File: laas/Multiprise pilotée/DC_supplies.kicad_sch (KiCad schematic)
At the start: 22 parts, among them J7 Conn_02x06_Odd_Even, Q1 DMN2020LSN-7, Q2 DMN2020LSN-7, Q3 SSM3J355R,LF, Q4 DMN2020LSN-7, Q5 DMN2020LSN-7, Q6 SSM3J355R,LF, Q7 DMN2020LSN-7, Q8 DMN2020LSN-7, U2 74HC595, U4 TC4469, U5 TC4469, U6 TDA7391PD, U7 74AHC1G08

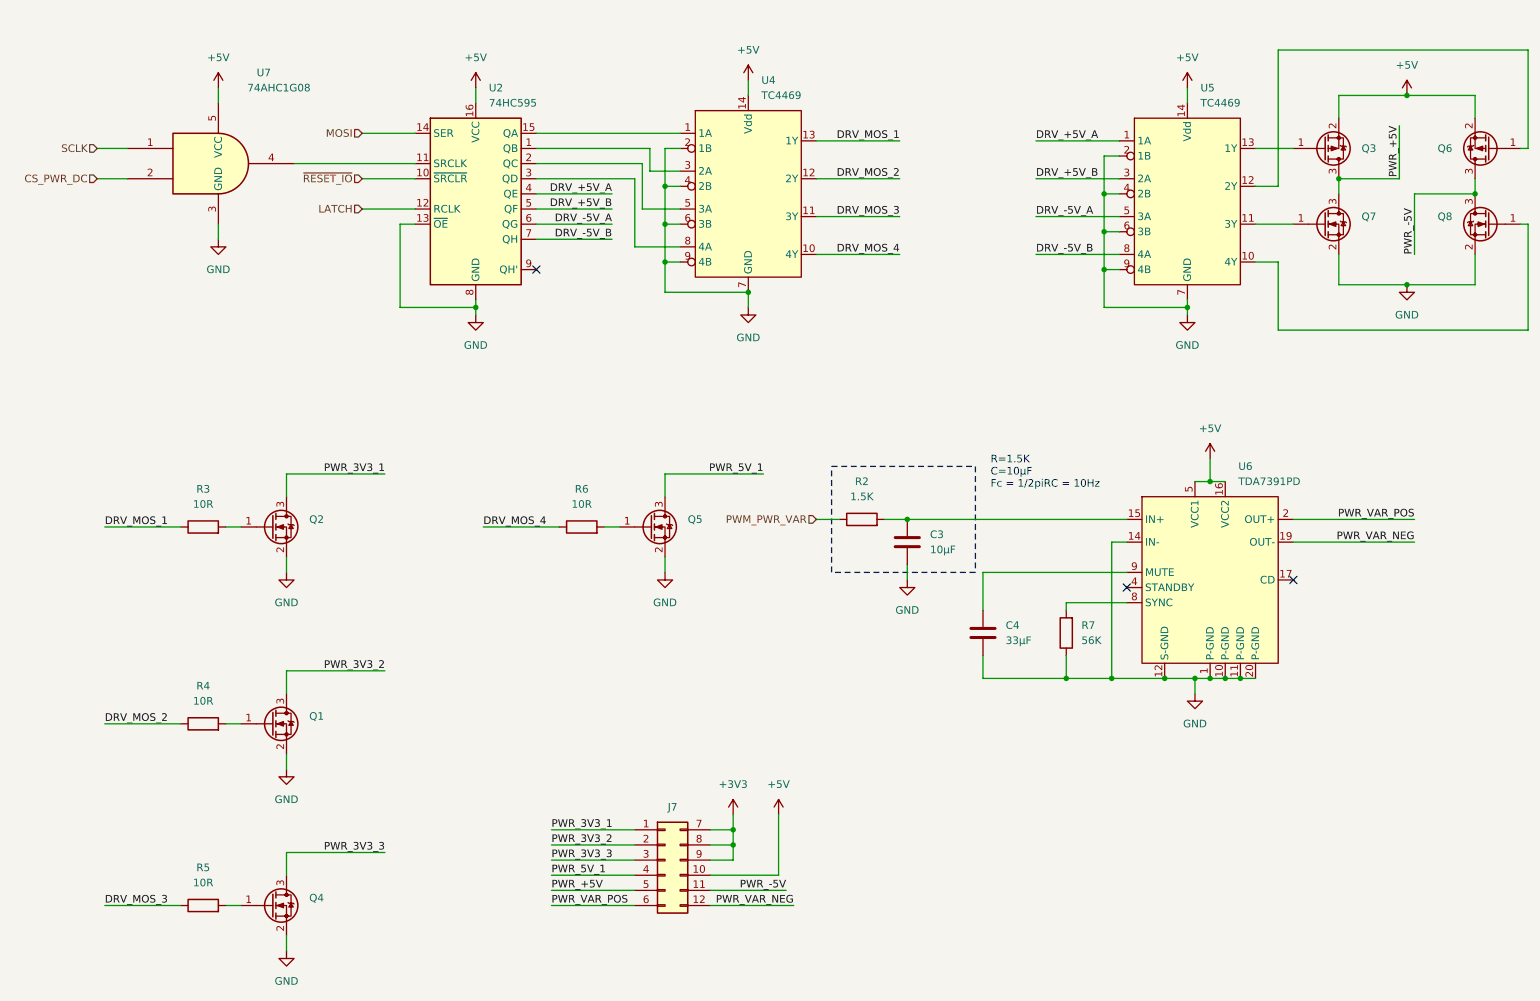
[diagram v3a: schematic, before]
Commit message: Nouvelle version PCB multiprise 1.3 avec suppresion des alim vpol et var
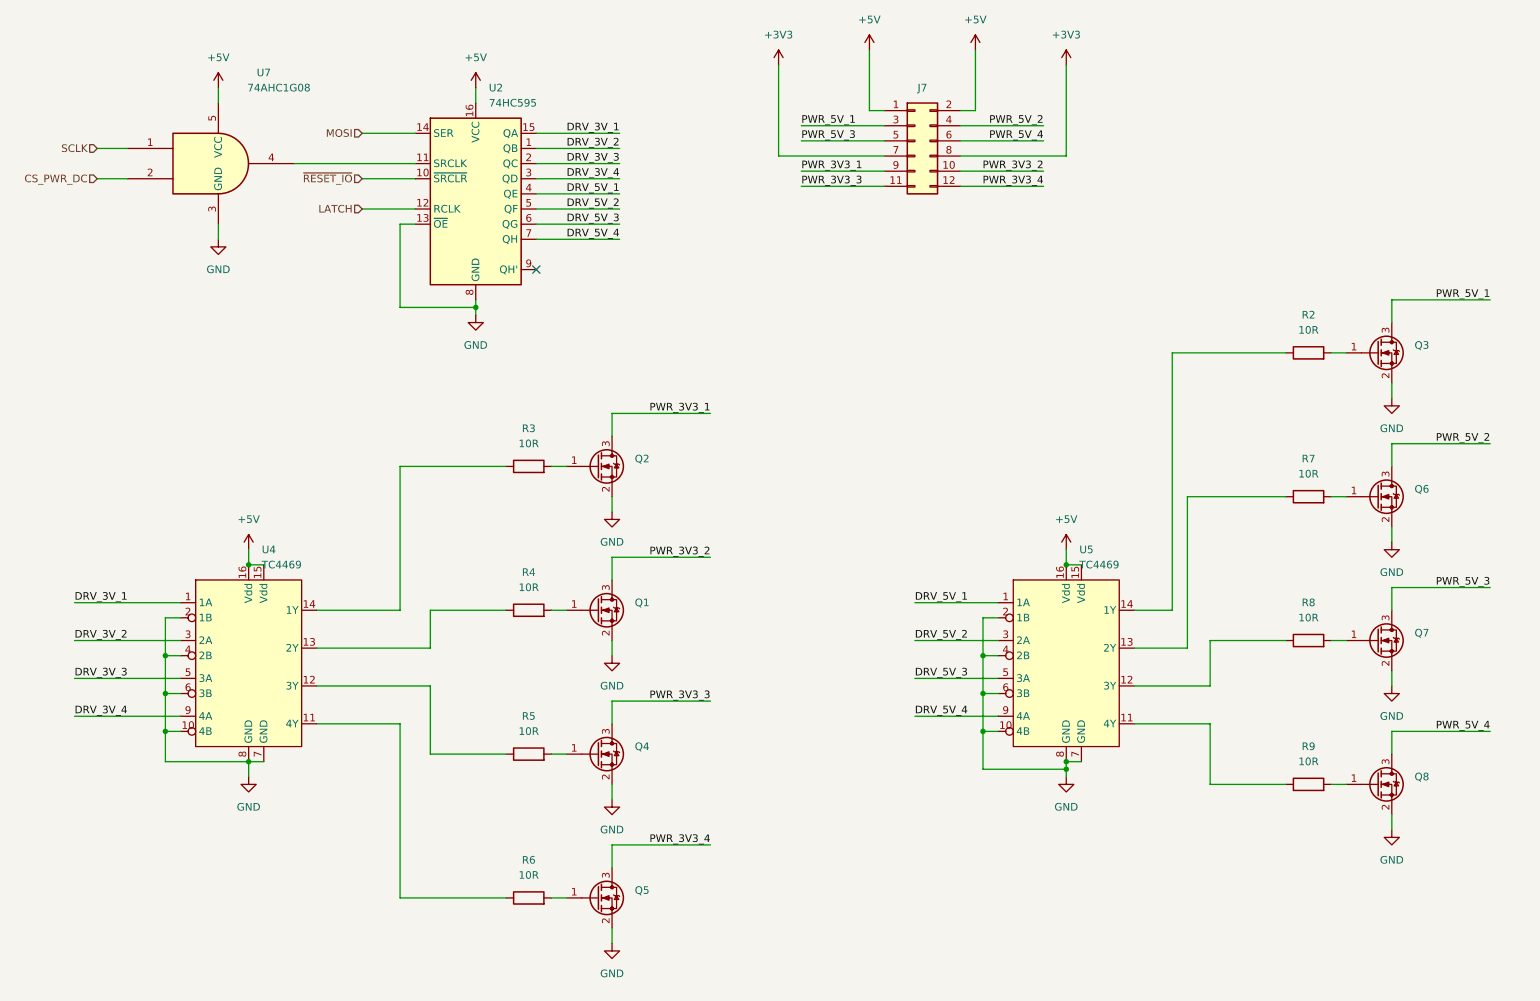
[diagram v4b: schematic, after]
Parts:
- removed C3: 10µF, Capacitor_SMD:C_1206_3216Metric, symbol Device:C
- removed C4: 33µF, Capacitor_SMD:C_1206_3216Metric, symbol Device:C
- removed Q3, Q6: SSM3J355R,LF, Package_TO_SOT_SMD:SOT-23, symbol Device:Q_PMOS_GSD
- removed U6: TDA7391PD, footprints:SO_91PDTR_STM, symbol Multiprise pilotée:TDA7391PD
- added Q3, Q6: DMN2020LSN-7, Package_TO_SOT_SMD:SC-59, symbol Device:Q_NMOS_GSD
- added R8, R9: 10R, Resistor_SMD:R_1206_3216Metric, symbol Device:R
- J7: footprint Borniers:M80-85312YY -> Connector_PinSocket_2.54mm:PinSocket_2x06_P2.54mm_Horizontal; symbol Connector_Generic:Conn_02x06_Top_Bottom -> Connector_Generic:Conn_02x06_Odd_Even
- Q1, Q2, Q4, Q5, Q7, Q8: value DMN2020LSN-7 -> DMN2020LSN-7
- R2: value 1.5K -> 10R
- R7: value 56K -> 10R
- U4, U5: footprint Package_SO:SOIC-14W_7.5x9mm_P1.27mm -> Package_SO:SOIC-16W_7.5x10.3mm_P1.27mm
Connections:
- net PWR_VAR_POS is gone; now on net PWR_5V_4: J7.6 (Pin_6)
- net +3V3: no longer J7.9 (Pin_9)
- net +5V: now also J7.1 (Pin_1), J7.2 (Pin_2), U4.15 (Vdd), U4.16 (Vdd), U5.15 (Vdd), U5.16 (Vdd); no longer J7.10 (Pin_10), U4.14 (Vdd), U5.14 (Vdd)
- net GND: now also U4.10 (4B), U4.8 (GND), U5.10 (4B), U5.8 (GND), Q3.2 (S), Q6.2 (S); no longer R7.1, U4.9 (4B), U5.9 (4B)
- net PWR_3V3_1: now also J7.9 (Pin_9); no longer J7.1 (Pin_1)
- net PWR_3V3_2: now also J7.10 (Pin_10); no longer J7.2 (Pin_2)
- net PWR_3V3_3: now also J7.11 (Pin_11); no longer J7.3 (Pin_3)
- net PWR_5V_1: now also J7.3 (Pin_3), Q3.3 (D); no longer J7.4 (Pin_4), Q5.3 (D)
- net at R7.2: now also Q6.1 (G)
- net at R2.2: now also Q3.1 (G)
- net DRV_3V_2: now reaches U2.1 (QB), U4.3 (2A)
- net DRV_3V_1: now reaches U2.15 (QA), U4.1 (1A)
- net DRV_3V_3: now reaches U2.2 (QC), U4.5 (3A)
- net DRV_3V_4: now reaches U2.3 (QD)
- net DRV_3V_4: now also U4.9 (4A); no longer U4.8 (4A)
- net at U5.12 (3Y): now also R8.1
- net at Q8.1 (G): now also R9.2; no longer U5.10 (4Y)
- net at Q7.1 (G): now also R8.2; no longer U5.11 (3Y)
- net at U5.13 (2Y): now also R7.1
- net DRV_+5V_A renamed DRV_5V_1
- net DRV_+5V_B renamed DRV_5V_2
- net DRV_-5V_A renamed DRV_5V_3
- net DRV_-5V_B renamed DRV_5V_4
- net DRV_5V_4: now also U5.9 (4A); no longer U5.8 (4A)
- net DRV_MOS_1: no longer names the net of R3.1
- net DRV_MOS_1: now also U4.14 (1Y); no longer U4.13 (1Y)
- net DRV_MOS_2: no longer names the net of U4.12 (3Y)
- net DRV_MOS_2: now also R5.1; no longer R4.1
- net DRV_MOS_3: no longer names the net of U4.11 (4Y)
- net DRV_MOS_3: now also R6.1; no longer R5.1
- removed net DRV_MOS_4: R6.1, U4.10 (4Y)
- net PWM_PWR_VAR: no longer names the net of R2.1
- net PWM_PWR_VAR: now also U5.14 (1Y)
- net PWR_+5V renamed PWR_5V_3
- net PWR_-5V renamed PWR_5V_4
- net PWR_5V_4: no longer J7.11 (Pin_11)
- net PWR_VAR_NEG renamed PWR_3V3_4
- net PWR_3V3_4: now also Q5.3 (D)
- new net: R9.1, U5.11 (4Y)
- new net: R4.1, U4.13 (2Y)
- new net PWR_5V_2: J7.4 (Pin_4), Q6.3 (D)
- no-connect marks 3 -> 1
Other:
- note removed: "R=1.5K C=10µF Fc = 1/2piRC = 10Hz"
- company: (none) -> INSA - GEI
- title: (none) -> Multiprise - Alimentations DC
- moved on the sheet: J7, Q1, Q2, Q4, Q5, R3, R4, R5, R6
